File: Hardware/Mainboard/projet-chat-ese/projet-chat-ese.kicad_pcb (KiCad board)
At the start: 4 copper layers, 58.5 x 45 mm, 93 parts, among them J201 Conn_01x06_Socket, J401 Conn_ST_STDC14, J402 USB_C_Receptacle_USB2.0_16P, J403 UART, J501 Conn_01x04, J502 Conn_01x04, J503 Conn_01x04, J504 Conn_01x04, J601 Conn_01x06_Socket, SW401 SW_SPST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

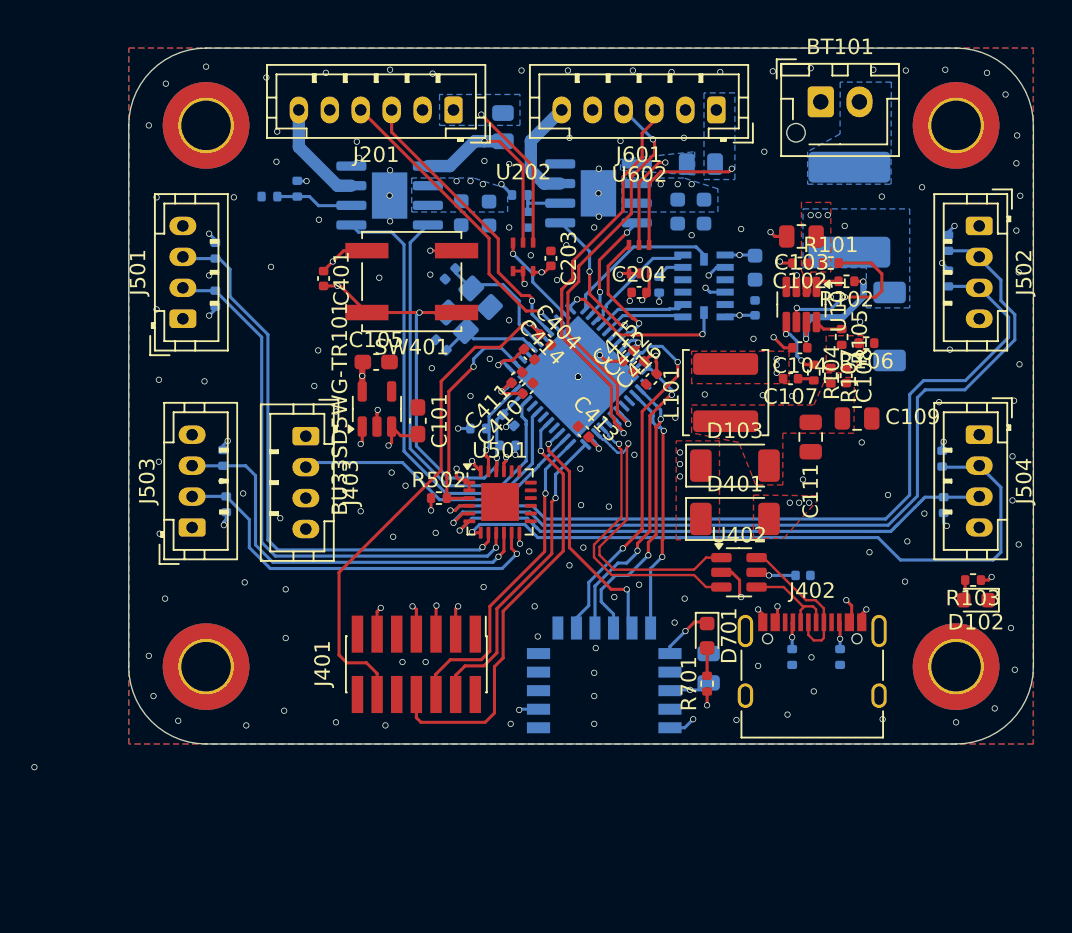
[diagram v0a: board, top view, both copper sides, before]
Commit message: Updating silkscreen on pcb
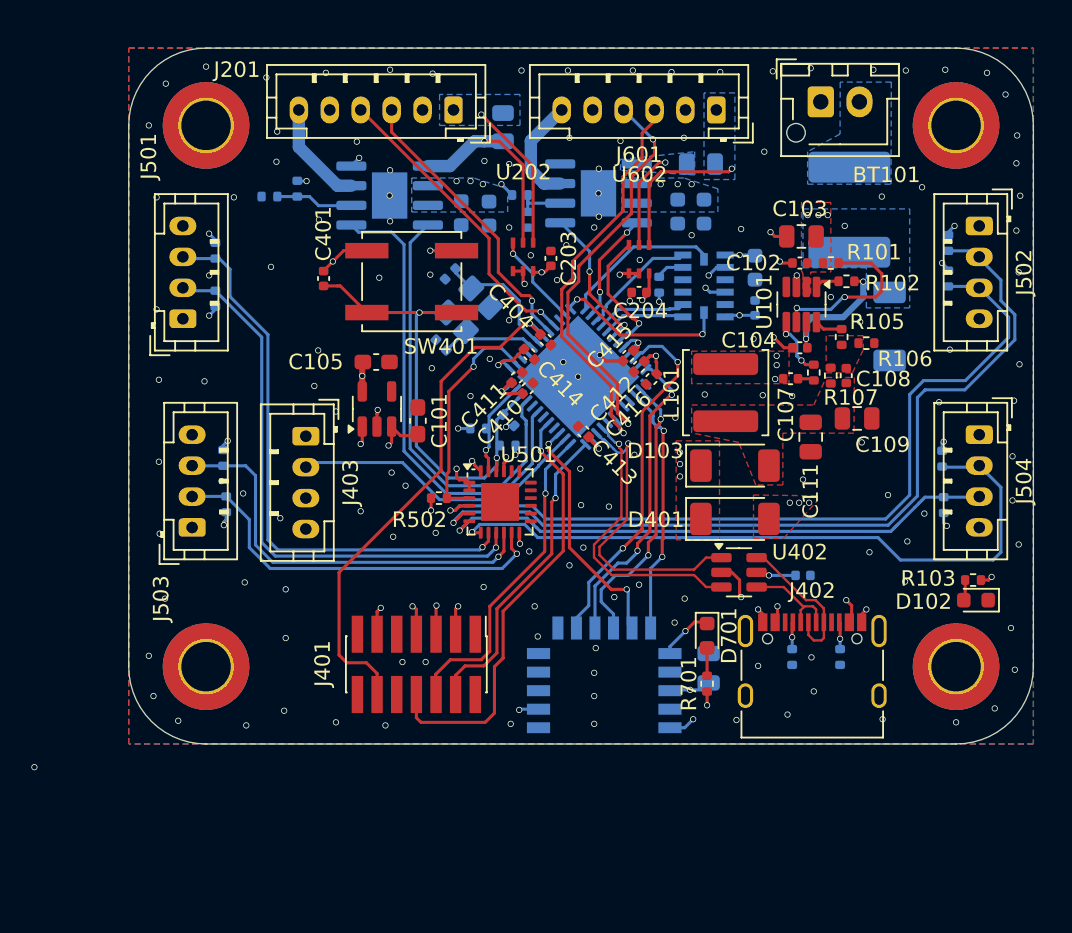
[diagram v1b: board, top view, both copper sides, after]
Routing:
- net GND: vias 166 -> 165
- net /MCU/ToF_SCL: vias 3 -> 2

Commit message: check pcb kenny LF
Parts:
- removed C401: 10n, Capacitor_SMD:C_0402_1005Metric
- removed R201, R202, R601, R602: R_Small, Resistor_SMD:R_0402_1005Metric
- removed R401: 100k, Resistor_SMD:R_0402_1005Metric
- removed SW401: SW_SPST, Button_Switch_SMD:SW_Push_1P1T_NO_CK_KSC6xxJ
- added L1: 39n, Inductor_SMD:L_0603_1608Metric, F.Cu at (180.5, 63.5)
- added R1: 100k, Resistor_SMD:R_0402_1005Metric, F.Cu at (191.1, 95.3)
- added R2: 100k, Resistor_SMD:R_0402_1005Metric, F.Cu at (191.1, 97.3)
- added R3: 100k, Resistor_SMD:R_0402_1005Metric, F.Cu at (196.0, 99.8)
- moved C416 1.13 mm to (178.0, 65.6), turned to -135 degrees
- moved C412 0.99 mm to (178.7, 66.3)
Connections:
- C415 pad 2: +3.3V -> /MCU/STM32_VDDA
- C416 pad 1: GND -> /MCU/STM32_VDDA
- C416 pad 2: +3.3V -> GND
- U201 pad 6: Net-(U201-VREF) -> +BATT
- U202 pad 1: GND -> /MOTOR_VREF
- U401 pad 21: +3.3V -> /MCU/STM32_VDDA
- U401 pad 32: unconnected-(U401-PA10-Pad32) -> /BT_Module/BLE_CONFIG
- U601 pad 6: Net-(U601-VREF) -> +BATT
- U602 pad 1: GND -> /MOTOR_VREF
- U701 pad 16: +3.3V -> /BT_Module/BLE_CONFIG
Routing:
- net +BATT: track 1.59 -> 10.3 mm
- net /MCU/STM32_VDDA: track 0.00 -> 6.29 mm, vias 0 -> 1
- net Net-(U201-VREF): track 5.04 -> 0.00 mm
- net +3.3V: track 45.3 -> 40.9 mm, vias 28 -> 25
- net Net-(U601-VREF): track 3.71 -> 0.00 mm
- net /BT_Module/BLE_CONFIG: track 0.00 -> 1.73 mm, vias 0 -> 1
- net /BT_Module/BT_UART_RX: track 23.4 -> 22.5 mm

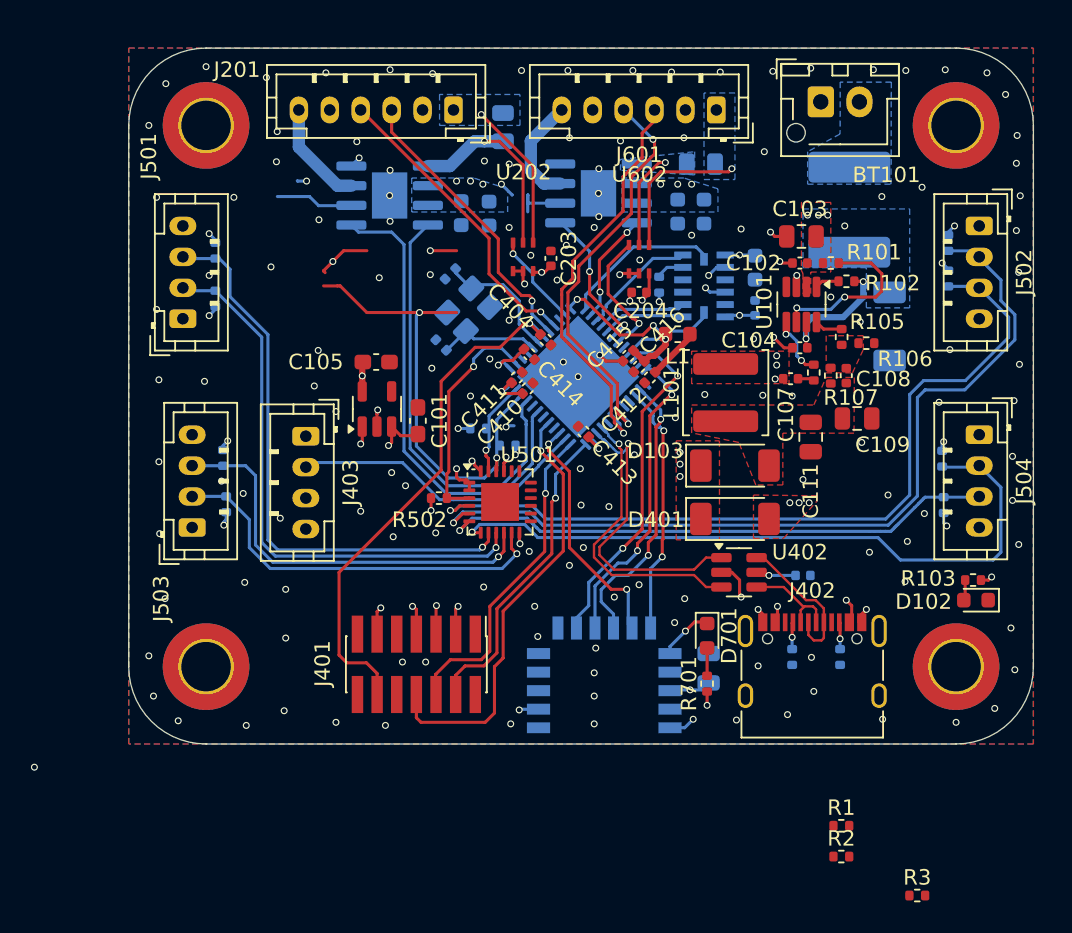
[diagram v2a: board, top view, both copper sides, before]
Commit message: Last PCB edits G431
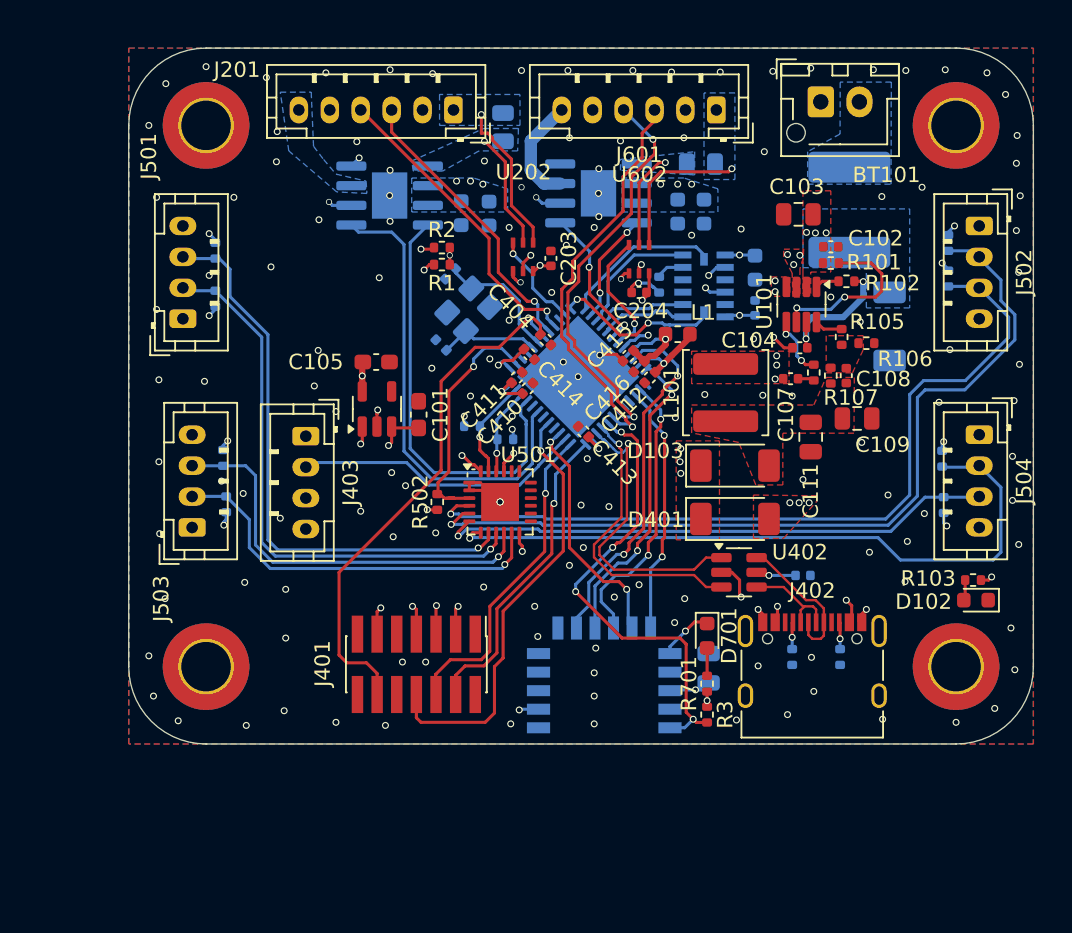
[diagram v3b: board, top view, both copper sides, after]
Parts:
- moved R2 47.1 mm to (165.2, 57.9), turned to 180 degrees
- moved R1 44.5 mm to (165.2, 59.0)
- moved R3 17.9 mm to (182.4, 88.1), turned to -90 degrees
- moved C102 2.26 mm to (190.4, 57.9), turned to 0 degrees
- moved C103 1.44 mm to (188.3, 55.8)
- moved R503 0.43 mm to (169.3, 70.3)
- moved R501 0.43 mm to (167.2, 69.5)
- moved C101 0.40 mm to (163.8, 68.7)
- moved R502 0.27 mm to (164.9, 74.3), turned to 90 degrees
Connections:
- U501 pad 25: (no net) -> GND
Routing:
- net /BT_Module/BLE_CONFIG: track 1.73 -> 30.2 mm, vias 1 -> 4
- net /MCU/ToF_SCL: track 30.5 -> 5.60 mm, vias 2 -> 1
- net +BATT: track 10.3 -> 3.24 mm
- net /Motor Sheet/MOT-: track 6.83 -> 0.00 mm
- net /Motor Sheet/MOT+: track 13.7 -> 7.61 mm
- net /MOTOR_VREF: track 0.00 -> 3.35 mm, vias 0 -> 3
- net /MCU/ToF_~{Reset}: track 14.5 -> 16.1 mm
- net +3.3V: track 40.9 -> 39.6 mm, vias 25 -> 26
- net GND: track 29.5 -> 30.7 mm, vias 165 -> 160
- net /MCU/NRST: track 34.3 -> 35.3 mm
- net /MCU/MOT1_REV: track 31.0 -> 30.3 mm
- net /MCU/UART1_Rx: track 19.5 -> 18.8 mm
- net /BT_Module/BT_UART_RX: track 22.5 -> 23.3 mm
- net /Accelerometer/ACC_SDIO: track 7.57 -> 8.35 mm
- net Net-(U101-SW): track 0.75 -> 0.00 mm, vias 4 -> 6
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- added copper zone on In2.Cu, net /MOTOR_VREF
- added copper zone on B.Cu, net /Motor Sheet/MOT+
- added copper zone on B.Cu, net /Motor Sheet/MOT-

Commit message: G431
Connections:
- J403 pad 3: GND -> /MCU/Lidar_speed
- U401 pad 44: unconnected-(U401-PB6-Pad44) -> /MCU/Lidar_speed
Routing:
- net /MCU/Lidar_speed: track 0.00 -> 17.3 mm, vias 0 -> 3
- net +3.3V: track 39.6 -> 40.2 mm
- net GND: vias 160 -> 159
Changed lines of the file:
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@@
 	(net 99 "/MCU/MOT1_FW")
 	(net 100 "Net-(U101-PG)")
-	(net 101 "unconnected-(U401-PB6-Pad44)")
+	(net 101 "/MCU/Lidar_speed")
 	(net 102 "unconnected-(U401-PB4-Pad42)")
 	(net 103 "unconnected-(U401-PA2-Pad10)")
@@
 			(layers "*.Cu" "*.Mask")
 			(remove_unused_layers no)
-			(net 1 "GND")
+			(net 101 "/MCU/Lidar_speed")
 			(pinfunction "Pin_3")
 			(pintype "passive")
@@
 		(at 170.5 58.5)
 		(property "Reference" "U202"
-			(at 0.025 -5.475 0)
+			(at 0.15 -2.15 0)
 			(unlocked yes)
 			(layer "F.SilkS")
@@
 		(at 178 58.65)
 		(property "Reference" "U602"
-			(at 0.025 -5.475 0)
+			(at 0.1 -2.3 0)
 			(unlocked yes)
 			(layer "F.SilkS")
@@
 			(layers "B.Cu" "B.Mask" "B.Paste")
 			(roundrect_rratio 0.25)
-			(net 101 "unconnected-(U401-PB6-Pad44)")
+			(net 101 "/MCU/Lidar_speed")
 			(pinfunction "PB6")
-			(pintype "bidirectional+no_connect")
+			(pintype "bidirectional")
 		)
 		(pad "45" smd roundrect
@@
 	)
 	(via
-		(at 169.8 68.8)
-		(size 0.45)
-		(drill 0.3)
-		(layers "F.Cu" "B.Cu")
-		(free yes)
-		(net 1)
-	)
-	(via
 		(at 162 72.45)
 		(size 0.45)
@@
 	)
 	(via
-		(at 169.8 69.65)
+		(at 169.325 69.265045)
 		(size 0.45)
 		(drill 0.3)
@@
 	)
 	(segment
-		(start 169.86 70.3)
-		(end 169.86 69.71)
+		(start 166.69 68.81)
+		(end 166.7 68.8)
 		(width 0.2)
 		(layer "B.Cu")
@@
 	)
 	(segment
-		(start 166.69 68.81)
-		(end 166.7 68.8)
+		(start 181.65 86.5)
+		(end 180.05257 86.5)
 		(width 0.2)
 		(layer "B.Cu")
@@
 	)
 	(segment
-		(start 181.65 86.5)
-		(end 180.05257 86.5)
+		(start 169.86 70.26)
+		(end 169.86 70.3)
 		(width 0.2)
 		(layer "B.Cu")
@@
 	)
 	(segment
+		(start 169.325 69.265045)
+		(end 169.325 69.725)
+		(width 0.2)
+		(layer "B.Cu")
+		(net 4)
+	)
+	(segment
 		(start 197.6 71.04)
 		(end 197.6 70.55)
@@
 	)
 	(segment
-		(start 169.86 69.71)
-		(end 169.8 69.65)
-		(width 0.2)
-		(layer "B.Cu")
-		(net 4)
-	)
-	(segment
 		(start 169.223413 67.2)
 		(end 169.687277 66.736136)
@@
 	)
 	(segment
+		(start 169.325 69.725)
+		(end 169.86 70.26)
+		(width 0.2)
+		(layer "B.Cu")
+		(net 4)
+	)
+	(segment
 		(start 197.6 70.55)
 		(end 197.7 70.45)
@@
 	)
 	(segment
-		(start 165.560589 64.539411)
-		(end 166.8 63.3)
+		(start 170 63.3)
+		(end 171.049651 64.349651)
 		(width 0.2)
 		(layer "B.Cu")
@@
 	)
 	(segment
-		(start 167.3 63.8)
-		(end 170.5 63.8)
+		(start 165.560589 64.539411)
+		(end 166.8 63.3)
 		(width 0.2)
 		(layer "B.Cu")
@@
 	)
 	(segment
-		(start 170.5 63.8)
-		(end 171.049651 64.349651)
+		(start 171.049651 64.349651)
+		(end 171.10149 64.349651)
 		(width 0.2)
 		(layer "B.Cu")
@@
 	(segment
 		(start 166.8 63.3)
-		(end 167.3 63.8)
-		(width 0.2)
-		(layer "B.Cu")
-		(net 13)
-	)
-	(segment
-		(start 171.049651 64.349651)
-		(end 171.10149 64.349651)
+		(end 170 63.3)
 		(width 0.2)
 		(layer "B.Cu")
@@
 	)
 	(segment
-		(start 167.7 71)
-		(end 168.075 71.375)
-		(width 0.2)
-		(layer "F.Cu")
-		(net 76)
-	)
-	(segment
 		(start 168.2625 71.5375)
 		(end 168.2625 72.3625)
@@
 	)
 	(segment
-		(start 167.7 70.15)
+		(start 167.7 70.45)
 		(end 167.7 71)
 		(width 0.2)
@@
 	)
 	(segment
-		(start 168.075 71.375)
-		(end 168.1 71.375)
+		(start 167.7 71)
+		(end 168.075 71.375)
 		(width 0.2)
 		(layer "F.Cu")
@@
 		(net 76)
 	)
+	(segment
+		(start 168.075 71.375)
+		(end 168.1 71.375)
+		(width 0.2)
+		(layer "F.Cu")
+		(net 76)
+	)
 	(via
-		(at 167.7 70.15)
+		(at 167.7 70.45)
 		(size 0.45)
 		(drill 0.3)
@@
 	)
 	(segment
-		(start 167.7 70.15)
-		(end 167.7 69.392482)
+		(start 170.04083 67.051652)
+		(end 170.04083 67.089689)
 		(width 0.2)
 		(layer "B.Cu")
@@
 	)
 	(segment
-		(start 170.04083 67.051652)
-		(end 170.04083 67.089689)
+		(start 167.7 70.45)
+		(end 167.7 69.392482)
 		(width 0.2)
 		(layer "B.Cu")
@@
 	)
 	(segment
-		(start 169.95 72.45)
-		(end 164.75 72.45)
-		(width 0.2)
-		(layer "B.Cu")
-		(net 99)
-	)
-	(segment
-		(start 170.747937 67.796796)
-		(end 170.35 68.194733)
+		(start 163.2 57.585)
+		(end 164.345 56.44)
 		(width 0.2)
 		(layer "B.Cu")
@@
 	)
 	(segment
-		(start 170.7 69.321774)
+		(start 170.7 70)
 		(end 170.7 71.7)
 		(width 0.2)
@@
 	)
 	(segment
-		(start 170.35 68.194733)
-		(end 170.35 68.75)
-		(width 0.2)
-		(layer "B.Cu")
-		(net 99)
-	)
-	(segment
-		(start 170.699 69.320774)
-		(end 170.7 69.321774)
+		(start 169.95 69.25)
+		(end 170.7 70)
 		(width 0.2)
 		(layer "B.Cu")
@@
 	)
 	(segment
-		(start 163.2 70.9)
-		(end 163.2 57.585)
+		(start 169.95 68.594733)
+		(end 169.95 69.25)
 		(width 0.2)
 		(layer "B.Cu")
@@
 	)
 	(segment
-		(start 163.2 57.585)
-		(end 164.345 56.44)
+		(start 163.2 70.9)
+		(end 163.2 57.585)
 		(width 0.2)
 		(layer "B.Cu")
@@
 	)
 	(segment
-		(start 170.35 68.75)
-		(end 170.699 69.099)
+		(start 169.95 72.45)
+		(end 164.75 72.45)
 		(width 0.2)
 		(layer "B.Cu")
@@
 	)
 	(segment
-		(start 170.699 69.099)
-		(end 170.699 69.320774)
+		(start 170.747937 67.796796)
+		(end 169.95 68.594733)
 		(width 0.2)
 		(layer "B.Cu")
@@
 	)
 	(segment
+		(start 164.525 70.825)
+		(end 161.25 74.1)
+		(width 0.2)
+		(layer "F.Cu")
+		(net 101)
+	)
+	(segment
+		(start 161.25 74.1)
+		(end 156.45 74.1)
+		(width 0.2)
+		(layer "F.Cu")
+		(net 101)
+	)
+	(segment
+		(start 170.575 69.047098)
+		(end 169.822098 69.8)
+		(width 0.2)
+		(layer "F.Cu")
+		(net 101)
+	)
+	(segment
+		(start 166.95 69.8)
+		(end 166.25 70.5)
+		(width 0.2)
+		(layer "F.Cu")
+		(net 101)
+	)
+	(segment
+		(start 169.822098 69.8)
+		(end 166.95 69.8)
+		(width 0.2)
+		(layer "F.Cu")
+		(net 101)
+	)
+	(via
+		(at 164.525 70.825)
+		(size 0.45)
+		(drill 0.3)
+		(layers "F.Cu" "B.Cu")
+		(net 101)
+	)
+	(via
+		(at 166.25 70.5)
+		(size 0.45)
+		(drill 0.3)
+		(layers "F.Cu" "B.Cu")
+		(net 101)
+	)
+	(via
+		(at 170.575 69.047098)
+		(size 0.45)
+		(drill 0.3)
+		(layers "F.Cu" "B.Cu")
+		(net 101)
+	)
+	(segment
+		(start 170.6 68.85)
+		(end 170.6 68.7)
+		(width 0.2)
+		(layer "B.Cu")
+		(net 101)
+	)
+	(segment
+		(start 170.575 68.875)
+		(end 170.6 68.85)
+		(width 0.2)
+		(layer "B.Cu")
+		(net 101)
+	)
+	(segment
+		(start 171.10149 68.19851)
+		(end 171.10149 68.150349)
+		(width 0.2)
+		(layer "B.Cu")
+		(net 101)
+	)
+	(segment
+		(start 164.525 70.825)
+		(end 164.85 70.5)
+		(width 0.2)
+		(layer "B.Cu")
+		(net 101)
+	)
+	(segment
+		(start 170.575 69.047098)
+		(end 170.575 68.875)
+		(width 0.2)
+		(layer "B.Cu")
+		(net 101)
+	)
+	(segment
+		(start 164.85 70.5)
+		(end 166.25 70.5)
+		(width 0.2)
+		(layer "B.Cu")
+		(net 101)
+	)
+	(segment
+		(start 170.6 68.7)
+		(end 171.10149 68.19851)
+		(width 0.2)
+		(layer "B.Cu")
+		(net 101)
+	)
+	(segment
 		(start 170 59.95)
 		(end 170.196732 60.146732)
@@
 			(pts
 				(xy 189.1 60.88) (xy 189.1 59.48) (xy 190.4 59.48) (xy 190.4 54.23) (xy 188.6 54.23) (xy 188.6 59.58)
-				(xy 188.6 59.58) (xy 188.6 60.88)
+				(xy 188.6 60.88)
 			)
 		)

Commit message: Kenny's Last work
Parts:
- moved J601 0.41 mm to (166.1, 49.4)
- renumbered J201 to J601, J601 to J602
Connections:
- J601 pad 1: /Motor Sheet/MOT+_OUT -> /Motor Sheet/MOT-
- J601 pad 2: GND -> +3.3V
- J601 pad 3: /MCU/MOT1_A -> /MCU/MOT1_B
- J601 pad 4: /MCU/MOT1_B -> /MCU/MOT1_A
- J601 pad 5: +3.3V -> GND
- J601 pad 6: /Motor Sheet/MOT- -> /Motor Sheet/MOT+_OUT
- J602 pad 1: /Motor Sheet1/MOT+_OUT -> /Motor Sheet1/MOT-
- J602 pad 2: GND -> +3.3V
- J602 pad 3: /MCU/MOT2_A -> /MCU/MOT2_B
- J602 pad 4: /MCU/MOT2_B -> /MCU/MOT2_A
- J602 pad 5: +3.3V -> GND
- J602 pad 6: /Motor Sheet1/MOT- -> /Motor Sheet1/MOT+_OUT
